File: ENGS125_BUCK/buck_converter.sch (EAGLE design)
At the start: 20 parts, among them M1 MOSFET_DPAK, M2 MOSFET_DPAK, U1 LTC4449, U2 LTC6992

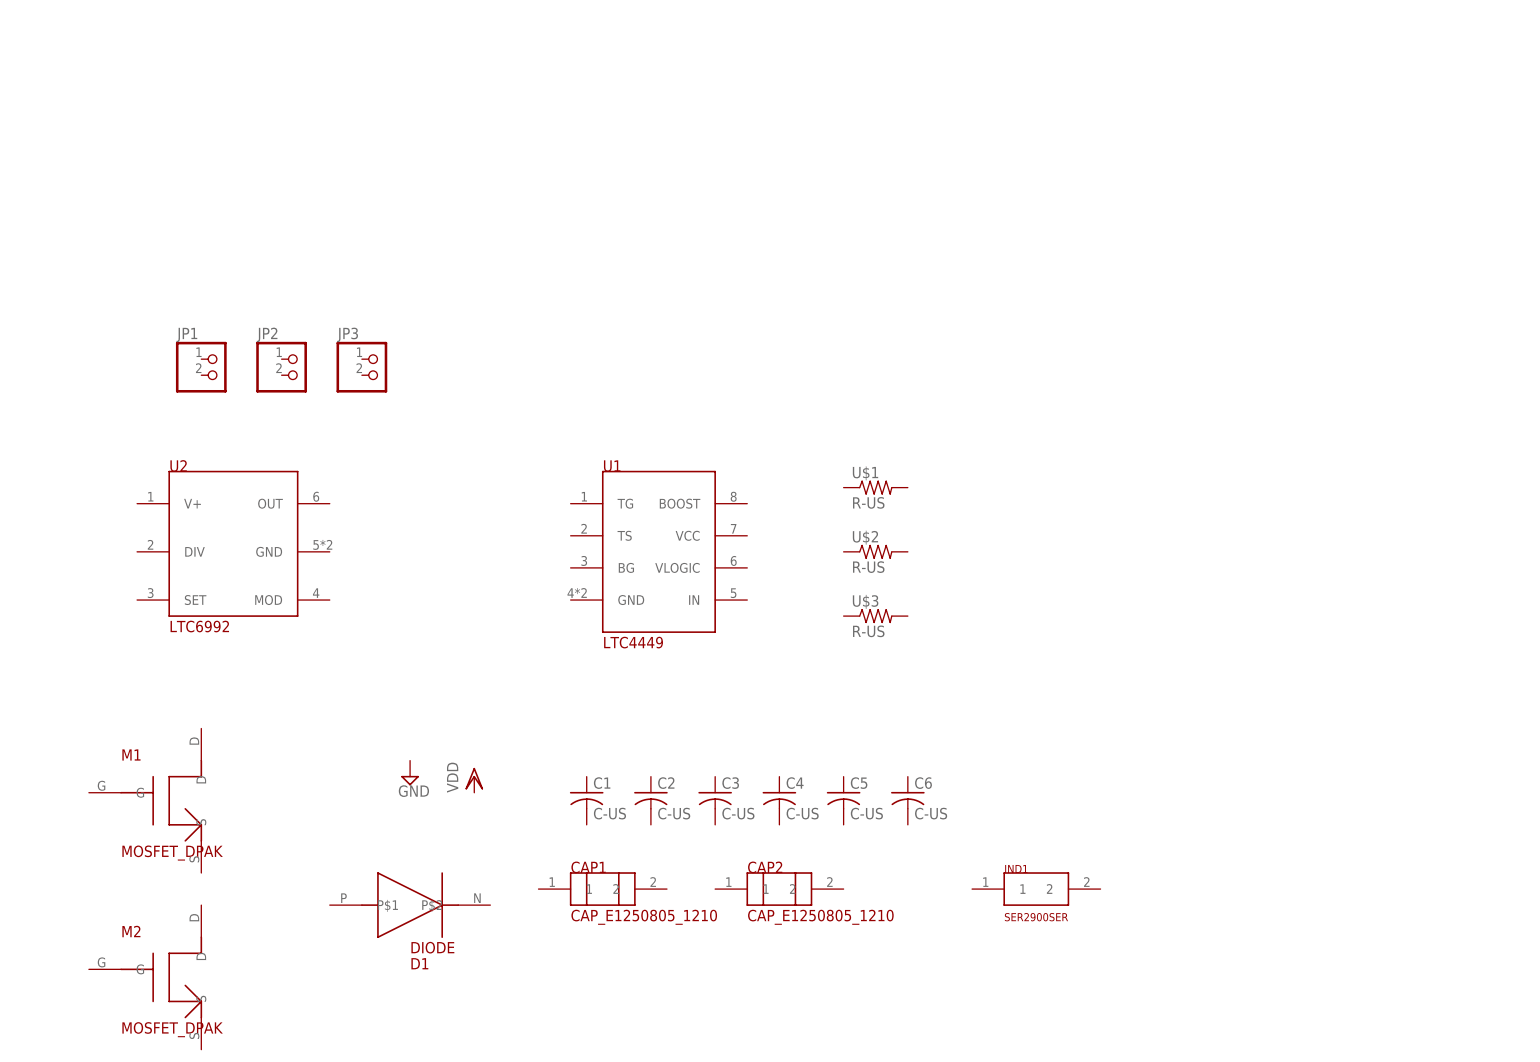
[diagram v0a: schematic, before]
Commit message: Completed schematic capture from LTSpice circuit
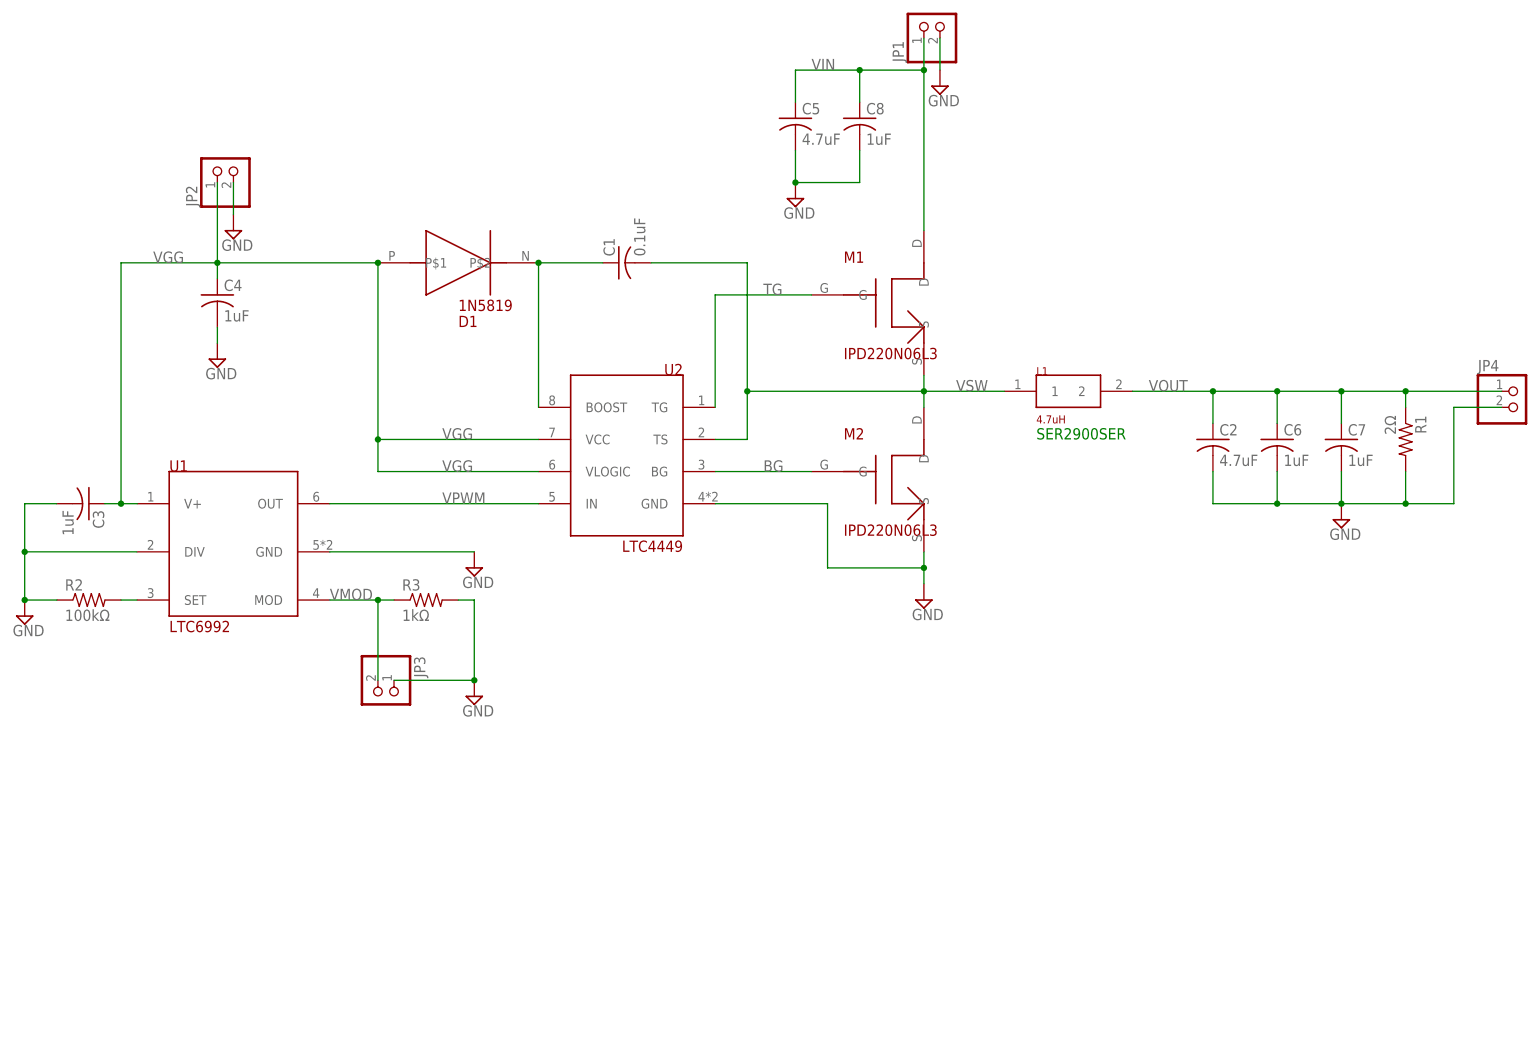
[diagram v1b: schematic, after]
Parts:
- removed CAP1, CAP2: CAP_E1250805_1210, Engs125_library:CAP_E1250805_1210
- removed IND1: SER2900SER, Engs125_library:SER2900SER
- removed U$1, U$2, U$3: R-US, Engs125_library:R-US
- added C7, C8: 1uF, Engs125_library:C-US
- added JP4: (no value), Engs125_library:PINHD-1X2
- added L1: 4.7uH, Engs125_library:SER2900SER
- added R1: 2Ω, Engs125_library:R-US
- added R2: 100kΩ, Engs125_library:R-US
- added R3: 1kΩ, Engs125_library:R-US
- C1: value C-US -> 0.1uF
- C2, C5: value C-US -> 4.7uF
- C3, C4, C6: value C-US -> 1uF
- D1: value DIODE -> 1N5819
- M1, M2: value MOSFET_DPAK -> IPD220N06L3
- U1: value LTC4449 -> LTC6992; device Engs125_library:LTC4449 -> Engs125_library:LTC6992
- U2: value LTC6992 -> LTC4449; device Engs125_library:LTC6992 -> Engs125_library:LTC4449
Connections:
- new net BG: M2.G, U2.BG
- new net GND: C2.2, C3.2, C4.2, C5.2, C6.2, C7.2, C8.2, JP1.2, JP2.2, JP3.1, JP4.2, M2.S, R1.2, R2.1, R3.2, U1.DIV, U1.GND, U2.GND
- new net N$1: R2.2, U1.SET
- new net N$2: C1.1, D1.P$2, U2.BOOST
- new net TG: M1.G, U2.TG
- new net VGG: C3.1, C4.1, D1.P$1, JP2.1, U1.V+, U2.VCC, U2.VLOGIC
- new net VIN: C5.1, C8.1, JP1.1, M1.D
- new net VMOD: JP3.2, R3.1, U1.MOD
- new net VOUT: C2.1, C6.1, C7.1, JP4.1, L1.2, R1.1
- new net VPWM: U1.OUT, U2.IN
- new net VSW: C1.2, L1.1, M1.S, M2.D, U2.TS
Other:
- note added: "SER2900SER"
- moved on the sheet: C1, C2, C3, C4, C5, C6, D1, JP1, JP2, JP3, M1, M2

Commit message: Removed load resistor and extraneous bypass capacitor in schematic
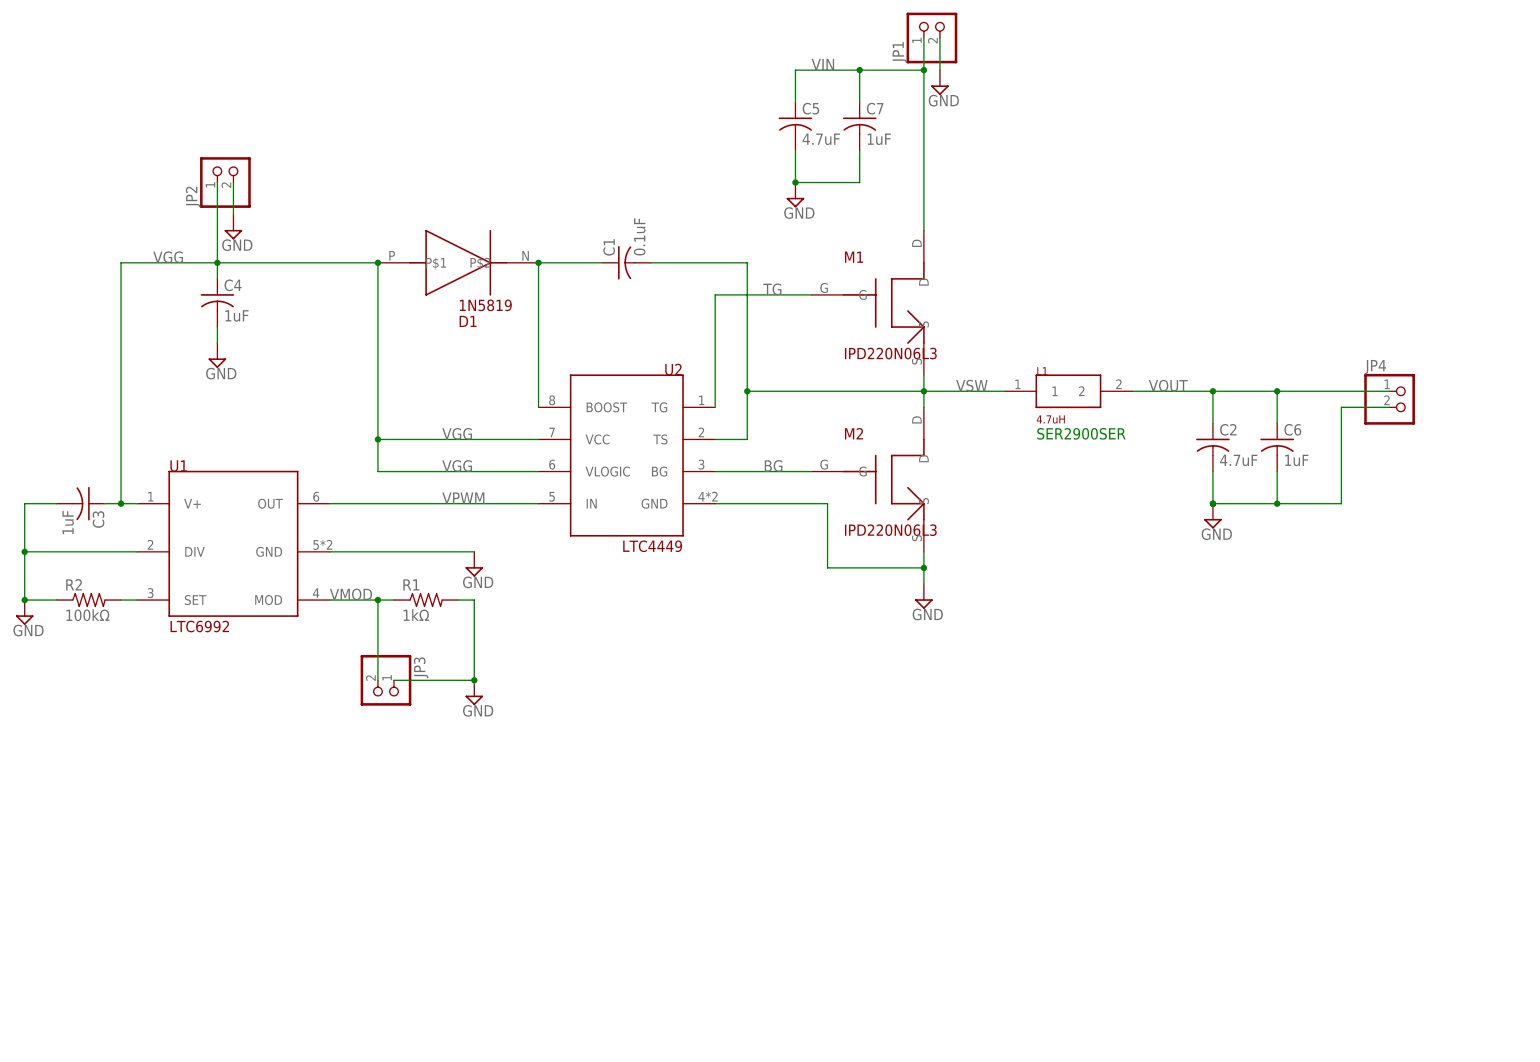
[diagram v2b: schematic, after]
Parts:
- removed C8: 1uF, Engs125_library:C-US
- removed R3: 1kΩ, Engs125_library:R-US
- C2, C5: device Engs125_library:C-US -> rcl:C-USC1206
- R1: value 2Ω -> 1kΩ
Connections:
- net GND: no longer C8.2, R3.2
- net VIN: now also C7.1; no longer C8.1
- net VMOD: now also R1.1; no longer R3.1
- net VOUT: no longer C7.1, R1.1
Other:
- moved on the sheet: C7, JP4, R1
